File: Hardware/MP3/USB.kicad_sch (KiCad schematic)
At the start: 11 parts, among them IC2 TUSB320LAIRWBR, J2 USB_C_Receptacle_USB2.0

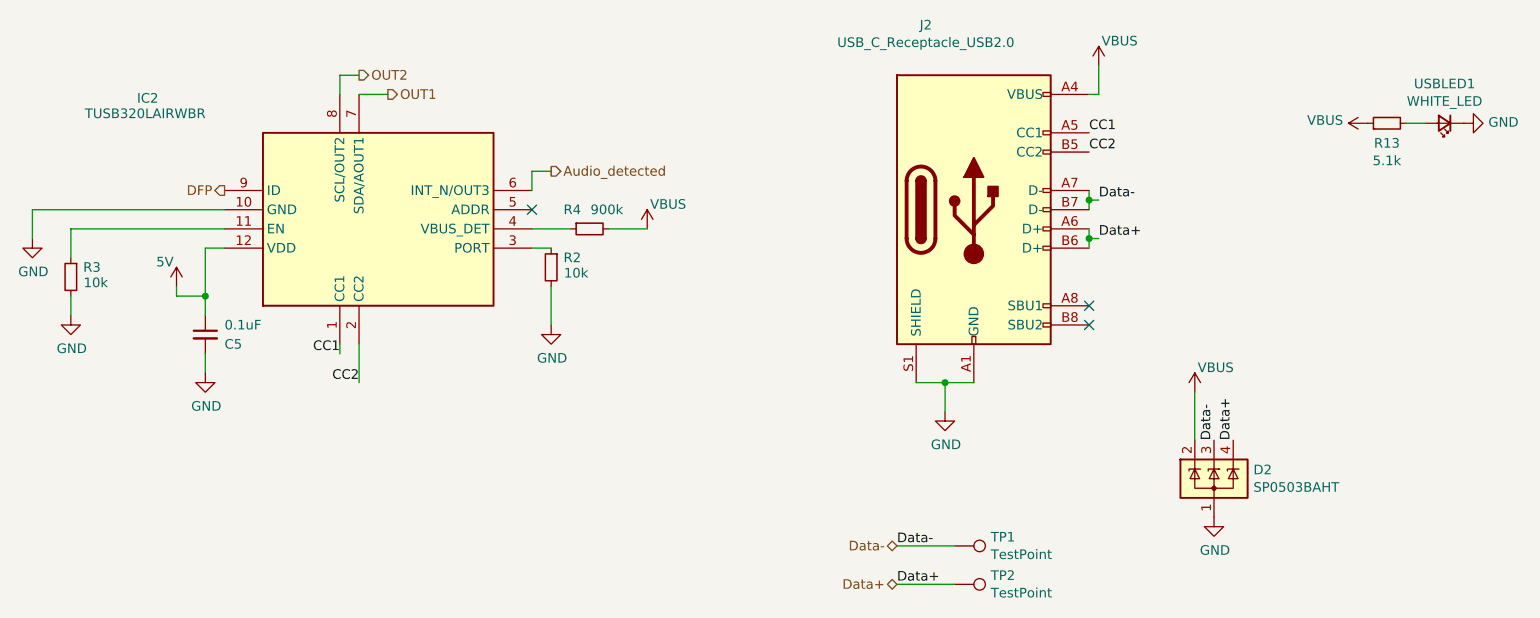
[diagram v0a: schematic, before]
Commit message: Large additions, DAC schematic work started
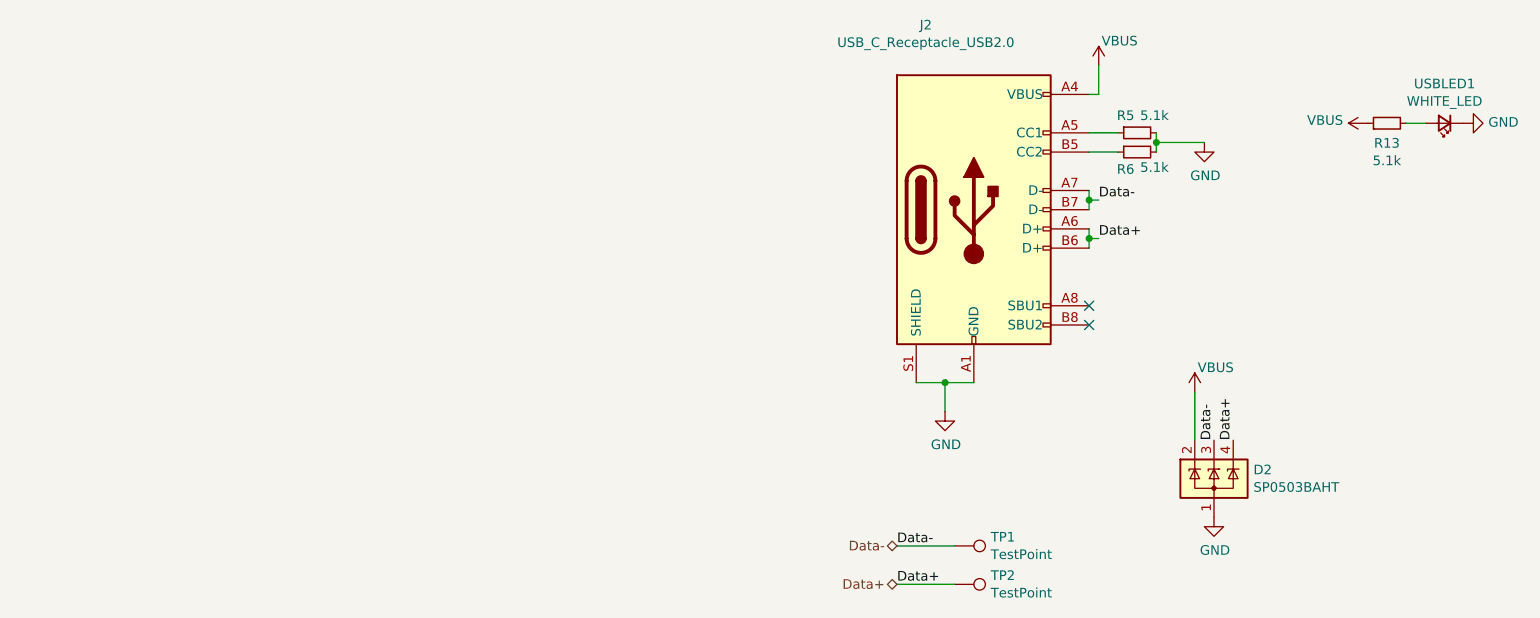
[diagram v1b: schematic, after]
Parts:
- removed C5: 0.1uF, Capacitor_SMD:C_0402_1005Metric, symbol Device:C_Small
- removed IC2: TUSB320LAIRWBR, iclr:RWB0012A, symbol iclr:TUSB320LAIRWBR
- removed R2, R3: 10k, Resistor_SMD:R_0402_1005Metric, symbol Device:R_Small
- removed R4: 900k, Resistor_SMD:R_0402_1005Metric, symbol Device:R_Small
- added R5, R6: 5.1k, Resistor_SMD:R_0402_1005Metric, symbol Device:R_Small
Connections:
- net GND: now also R5.2, R6.2
- net CC1: no longer names the net of J2.A5 (CC1)
- net CC1: now also R5.1
- net CC2: no longer names the net of J2.B5 (CC2)
- net CC2: now also R6.1
- no-connect marks 3 -> 2
